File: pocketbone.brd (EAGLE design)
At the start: 55 x 35 mm, 60 parts, among them J1 USD_CONNECTOR, U1 24LC_32AT-I/OT, U2 OSD3358, U3 SN74LVC1G07_DCK_5, Y1 CM200C-32.768KAZF-UT, Y2 445C33D24M00000

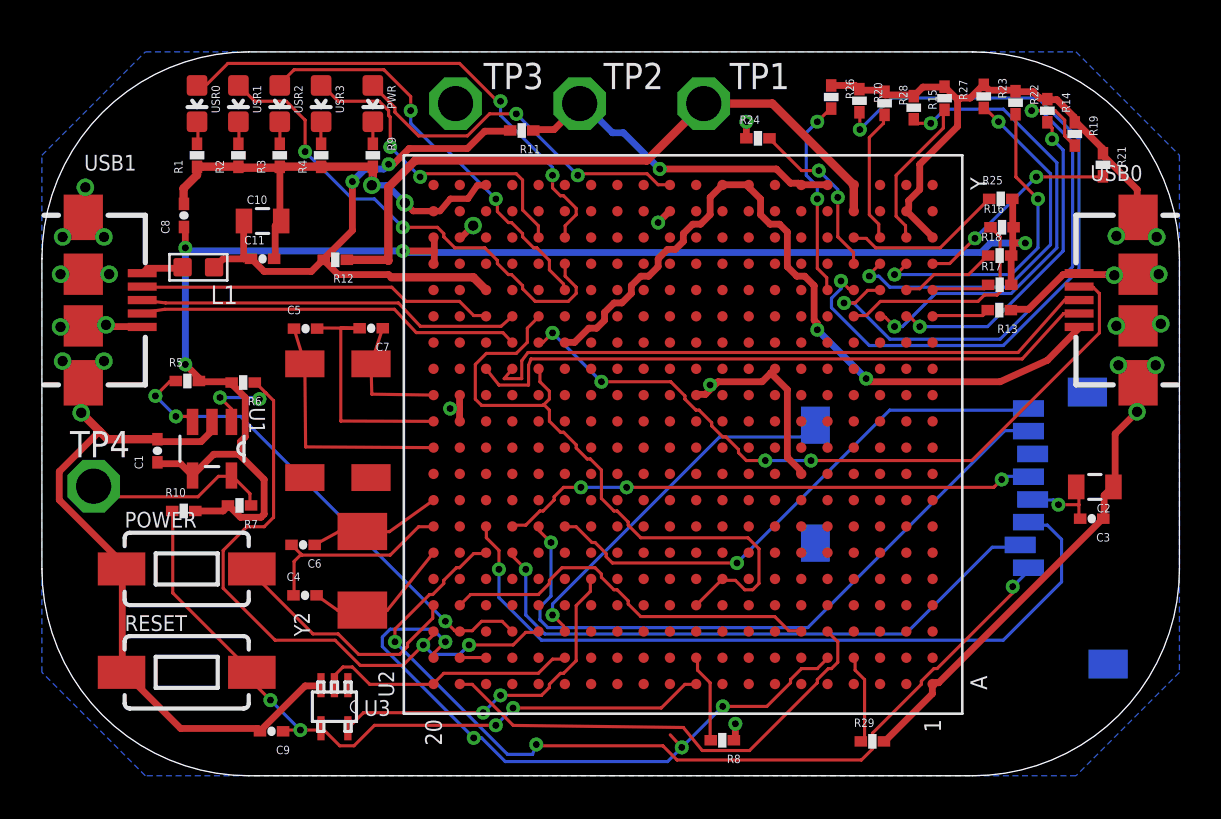
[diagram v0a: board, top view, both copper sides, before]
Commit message: Updated components to match BB Blue.
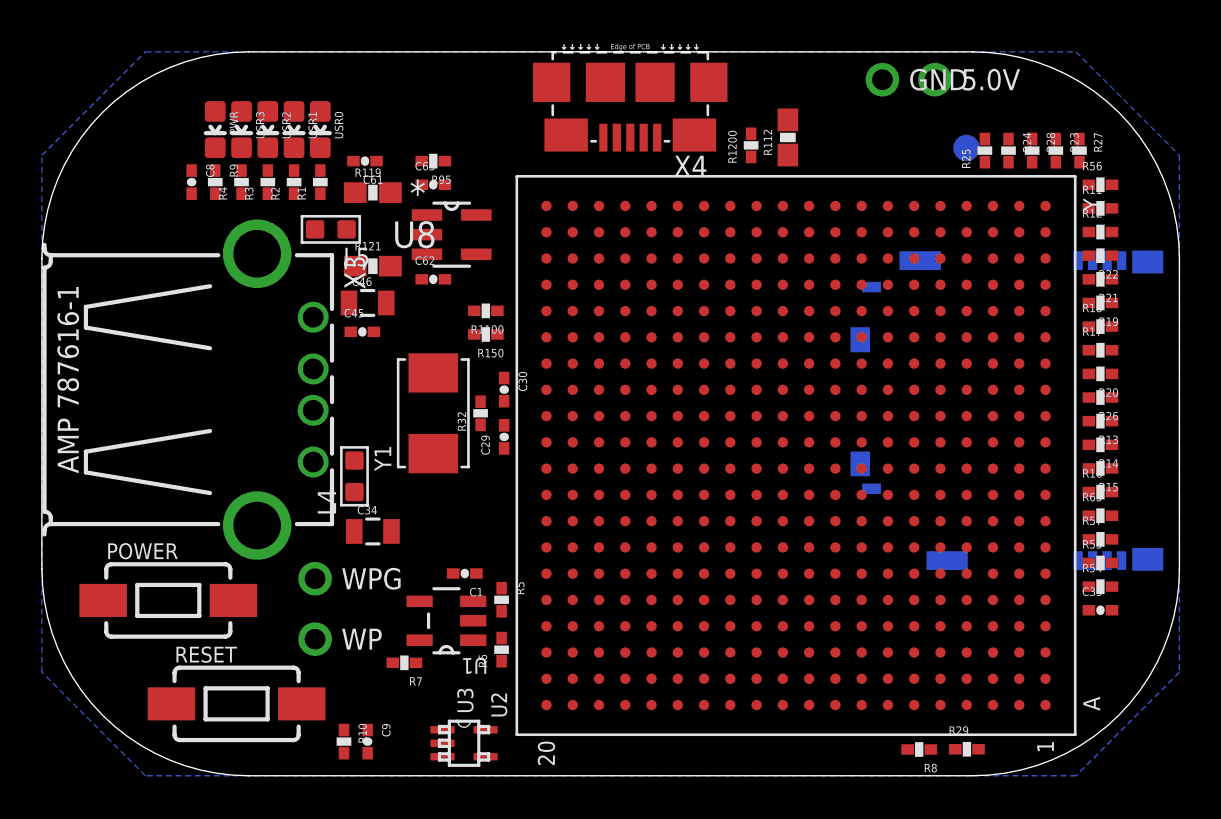
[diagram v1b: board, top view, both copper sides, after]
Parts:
- removed C10, C2: 10uF, Strawson_Eagle_Lib:0805
- removed C11, C3: 0.1uF, Strawson_Eagle_Lib:0402-CAP
- removed C4, C5, C6, C7: 20pF, Strawson_Eagle_Lib:0402-CAP
- removed J1: USD_CONNECTOR, pocketbone:MICRO-SD-SOCKET-PP
- removed L1: 120, Seeed-OPL-Inductor:L0603
- removed TP1, TP2, TP3, TP4: TPSQPAD1-17, pocketbone:P1-17
- removed USB0, USB1: USB-MICRO-SMD, pocketbone:USB-AB-MICRO-SMD
- removed Y2: 445C33D24M00000, pocketbone:445C33D24M00000
- added 5.0V, GND, WP, WPG: GHI_TESTPAD/W_HOLE_1X1, pocketbone:GHI2_TESTPAD/W_HOLE_1X1
- added C29, C30: 10pF, Strawson_Eagle_Lib:0402-CAP
- added C34, C46: 10uF, Strawson_Eagle_Lib:0805
- added C35, C45: 0.1uF, Strawson_Eagle_Lib:0402-CAP
- added C61: 1uF, Strawson_Eagle_Lib:0402-CAP
- added C62, C63: 0.22uF, Strawson_Eagle_Lib:0402-CAP
- added L4, L5: 120, Seeed-OPL-Inductor:L0603
- added R1100, R1200: 33, Strawson_Eagle_Lib:0402-RES
- added R112: 0, SparkFun-Resistors:0603-RES
- added R119, R121: 0, DNP, SparkFun-Resistors:0603-RES
- added R150: 0, Strawson_Eagle_Lib:0402-RES
- added R32: 1M, Strawson_Eagle_Lib:0402-RES
- added R54, R55, R56, R57, R65: 10K, Strawson_Eagle_Lib:0402-RES
- added R95: 100K, Strawson_Eagle_Lib:0402-RES
- added SYS_5V: TPSQB1,27, testpad:B1,27
- added U8: TPS2105_DBV_5, BeagleBone_Blue:DBV5
- added X2: SCHA5B0200, GHI-Connectors:SCHA5B0200
- added X3: USB1, GHI2:USB_HOST_HORIZONTAL_W/CHASSIS_GND
- added X4: 10118192-0001LF, GHI-Connectors:10118192-0001LF(MICRO-USB-B-AMPHENOL-FCI)
- R11: value 0 -> 10K
- R12: value 0,DNI -> 10K
- R8, R9: value 4.87k -> 4.7k
- Y1: value CM200C-32.768KAZF-UT -> 24 MHz; device pocketbone:CM200C-32.768KAZF-UT -> GHI2:CRYSTAL_5X3.2MM
- moved R12 37.0 mm to (51.2, 26.3), turned to 0 degrees
- moved R11 28.2 mm to (51.2, 27.4), turned to 0 degrees
- moved R15 19.6 mm to (51.2, 14.9), turned to 180 degrees
- moved R26 19.5 mm to (51.2, 18.3), turned to 180 degrees
- moved R5 18.5 mm to (22.2, 8.51), turned to 270 degrees
- moved R6 18.0 mm to (22.2, 6.10), turned to 90 degrees
- moved R20 17.6 mm to (51.2, 19.4), turned to 180 degrees
- moved R14 16.4 mm to (51.2, 16.0), turned to 180 degrees
- moved C1 16.0 mm to (20.4, 9.78), turned to 180 degrees
- moved U1 14.1 mm to (19.6, 7.49), turned to 180 degrees
- moved R16 13.7 mm to (51.2, 13.7)
- moved R10 13.6 mm to (14.6, 1.65), turned to 270 degrees
- moved R24 12.1 mm to (46.7, 30.2), turned to 270 degrees
- moved R7 11.0 mm to (17.5, 5.46)
- moved R8 9.53 mm to (42.4, 1.27)
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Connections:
- removed net N$129: C10.1, C11.1, L1.1, R11.2, R12.2, U2.T18
- removed net N$2: J1.CLK, U2.G17
- removed net N$32: C6.1, U2.H20, Y2.2
- removed net N$33: C4.2, U2.F20, Y2.1
- removed net N$34: C4.1, C6.2, U2.G20
- removed net N$5: J1.CD/DAT3, U2.F17
- removed net N$70: J1.DAT1, U2.G15
- removed net N$74: J1.CMD, U2.G18
- removed net N$75: J1.CD1, U2.C15
- removed net N$77: J1.DAT0, U2.G16
- removed net NTE: J1.DAT2, U2.F18
- removed net USB0_DM: U2.N18, USB0.D-
- removed net USB0_DP: U2.N17, USB0.D+
- removed net USB1_DM: U2.R18, USB1.D-
- removed net USB1_DP: U2.R17, USB1.D+
- removed net USB1_ID: U2.P17, USB1.ID
- new net CGND: X2.CGND1, X2.CGND2, X2.CGND3, X2.CGND4, X2.CGND5, X2.CGND6, X3.5, X3.6, X4.CGND1, X4.CGND2, X4.CGND3, X4.CGND4, X4.CGND5, X4.CGND6
- new net N$11: R1100.1, U2.T18
- new net N$126: R150.1, U2.P17
- new net N$128: L4.2, X3.4
- new net N$130: L5.2, X3.1
- new net N$3: R56.1, U2.G18, X2.3
- new net N$4: R55.1, U2.G16, X2.7
- new net N$6: R54.1, U2.G15, X2.8
- new net N$7: R65.1, U2.C15, X2.CD
- new net N$8: R57.1, U2.G17, X2.5
- new net N$9: R11.1, U2.F17, X2.2
- new net NTE1: R12.1, U2.F18, X2.1
- new net USB0_D_N: U2.N18, X4.D-
- new net USB0_D_P: U2.N17, X4.D+
- new net USB0_VBUS: R112.2, R1200.2, X4.VBUS
- new net USB1_D_N: U2.R18, X3.2
- new net USB1_D_P: U2.R17, X3.3
- new net USB1_VBUS: C45.1, C46.1, C61.2, L5.1, R1100.2, R119.1, R121.1, U8.4
- net 3.3V: now also C34.2, C35.2, R11.2, R12.2, R54.2, R55.2, R56.2, R57.2, R65.2, X2.4; no longer C2.2, C3.2, J1.VCC
- net 5.0V: now also 5.0V.P$1, C63.1, R119.2, R95.2, U8.1, U8.5; no longer R11.1, TP2.TP
- net GND: now also C34.1, C35.1, C45.2, C46.2, C61.1, C62.2, C63.2, GND.P$1, L4.1, R150.2, R95.1, U8.2, WPG.P$1, X2.6, X2.GND, X4.GND; no longer C10.2, C11.2, C2.1, C3.1, J1.GND, J1.GND1, J1.GND3, TP3.TP, USB0.GND, USB0.SHIELD1, USB0.SHIELD2, USB0.SHIELD3, USB0.SHIELD4, USB1.GND, USB1.SHIELD1, USB1.SHIELD2, USB1.SHIELD3, USB1.SHIELD4
- net N$1: now also R1200.1, U2.P15; no longer L1.2, USB1.VBUS
- net N$26: now also C30.1, R32.2; no longer C7.1
- net N$27: now also C29.1, R32.1; no longer C5.1
- net N$28: now also WP.P$1; no longer TP4.TP
- net N$31: now also C29.2, C30.2; no longer C5.2, C7.2
- net SYS_5V: now also C62.1, R121.2, SYS_5V.TP, U8.3; no longer R12.1, TP1.TP
- net USB0_ID: now also X4.ID; no longer USB0.ID
- net USB_DC: now also R112.1; no longer U2.P15, USB0.VBUS
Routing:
- net GND: track 137.6 -> 0.00 mm, vias 27 -> 0
- net 3.3V: track 77.6 -> 0.00 mm, vias 5 -> 0
- net NTE: track 44.9 -> 0.00 mm, vias 3 -> 0
- net N$74: track 37.0 -> 0.00 mm, vias 1 -> 0
- net USB_DC: track 36.9 -> 0.00 mm, vias 2 -> 0
- net SVO6: track 35.8 -> 0.00 mm, vias 2 -> 0
- net USB0_ID: track 35.7 -> 0.00 mm, vias 4 -> 0
- net RESET: track 34.9 -> 0.00 mm, vias 4 -> 0
- net I2C0_SCL: track 34.3 -> 0.00 mm, vias 4 -> 0
- net N$77: track 32.7 -> 0.00 mm, vias 1 -> 0
- net SYS_5V: track 32.7 -> 0.00 mm
- net VDD_1V8: track 31.8 -> 0.00 mm
- net LDO_PGOOD: track 31.8 -> 0.00 mm, vias 4 -> 0
- net USB0_DM: track 31.2 -> 0.00 mm
- net USB0_DP: track 30.7 -> 0.00 mm
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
